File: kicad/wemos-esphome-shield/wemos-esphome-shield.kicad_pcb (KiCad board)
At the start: 2 copper layers, 74 x 52 mm, 28 parts, among them Q1 2N2222, Q2 2N2222, Q3 2N2222, T1 Transformer_1P_1S, U1 WeMos_D1_mini

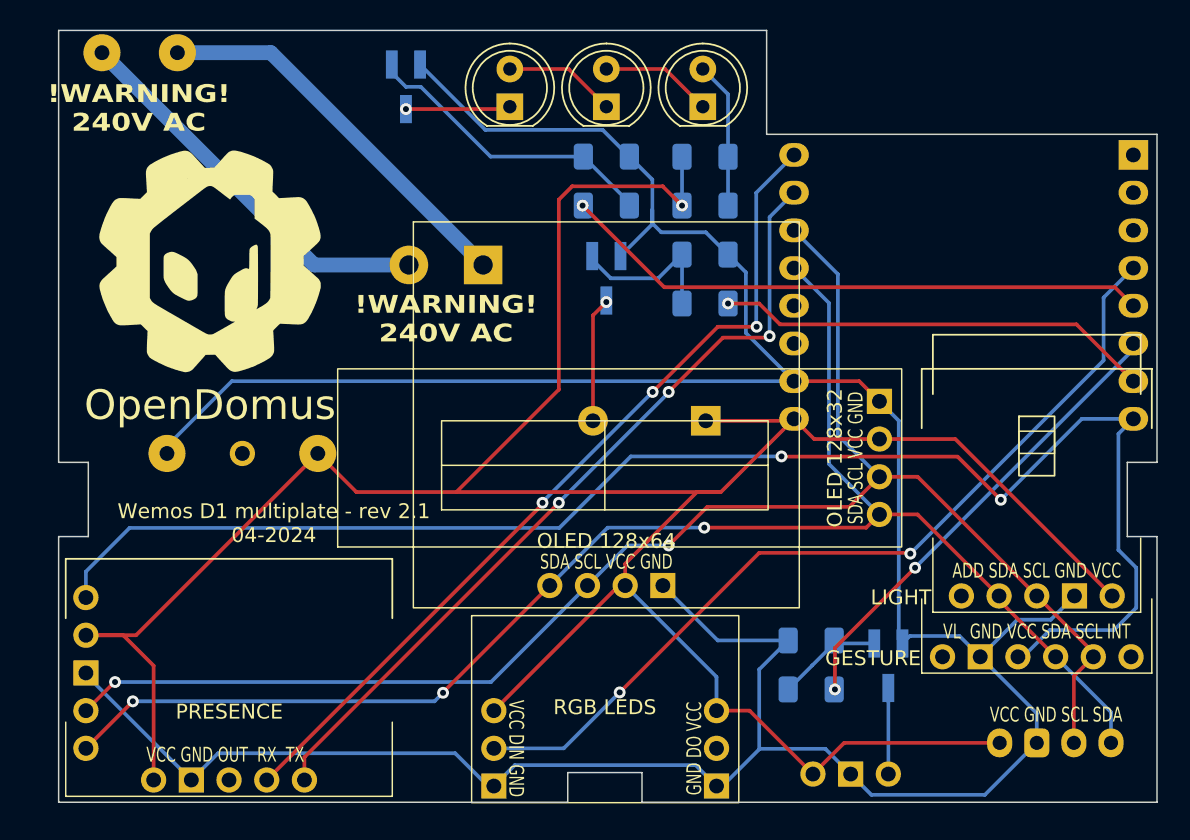
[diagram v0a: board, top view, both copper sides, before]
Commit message: move stuff around
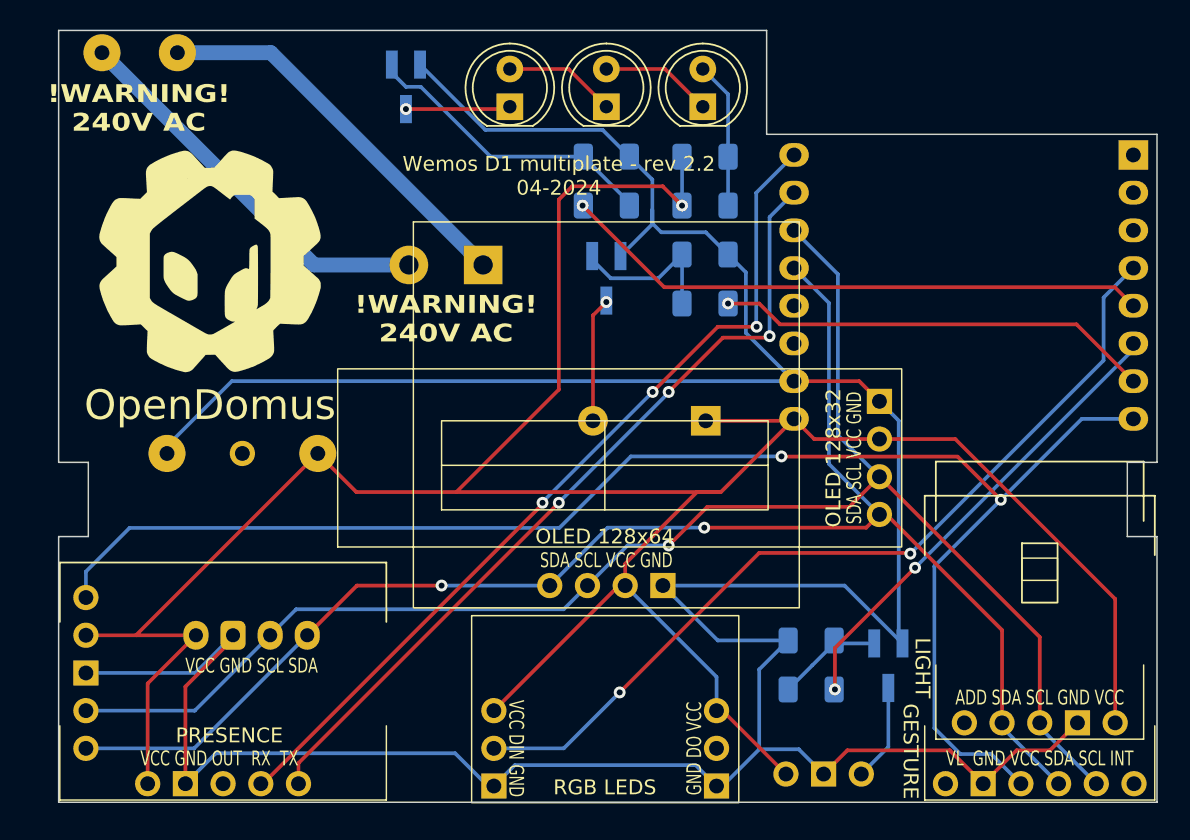
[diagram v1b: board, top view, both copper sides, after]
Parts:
- moved TEMP1 62.1 mm to (88.2, 104.8), turned to 0 degrees
- moved LUM1 8.55 mm to (145.1, 110.7)
- moved GEST1 8.55 mm to (145.1, 114.8)
- moved RELAY1 1.82 mm to (133.1, 114.1)
- moved MOV1 0.47 mm to (90.1, 114.8)
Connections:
- TEMP1 pad 1: SDA -> 5V
- TEMP1 pad 2: SCL -> GND
- TEMP1 pad 3: GND -> SCL
- TEMP1 pad 4: 5V -> SDA
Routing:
- net GND: track 222.3 -> 236.8 mm
- net 5V: track 192.7 -> 188.4 mm
- net 3.3V: track 102.0 -> 103.6 mm
- net SCL: track 104.9 -> 105.7 mm, vias 2 -> 1
- net Net-(Q2-C): track 5.80 -> 6.55 mm
- net SDA: vias 3 -> 2
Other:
- outline, holes or cut-outs redrawn
- board text added: "Wemos D1 multiplate - rev 2.2 04-2024"
- board text removed: "Wemos D1 multiplate - rev 2.1 04-2024"

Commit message: rev2.2 sent to jlcpcb
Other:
- board text added: "SDA SCL GND VCC"
- board text added: "TEMPERATURE/ HUMIDITY"
- board text removed: "TEMPERATURE"
- board text removed: "VCC GND SCL SDA"
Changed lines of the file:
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@@
     (effects (font (size 1 1) (thickness 0.15)) (justify right mirror))
   )
-  (gr_text "TEMPERATURE" (at 92 108.225) (layer "B.SilkS")
-    (effects (font (size 1 1) (thickness 0.15)) (justify mirror))
+  (gr_text "TEMPERATURE/\nHUMIDITY" (at 91.9 107.8) (layer "B.SilkS")
+    (effects (font (size 1 1) (thickness 0.15)) (justify top mirror))
   )
   (gr_text "RX" (at 129.8 75) (layer "B.SilkS")
@@
   (gr_text "3.3V" (at 150.3 90.2) (layer "B.SilkS")
     (effects (font (size 1 1) (thickness 0.15)) (justify left mirror))
+  )
+  (gr_text "SDA SCL GND VCC" (at 92 106.8) (layer "B.SilkS")
+    (effects (font (size 1 0.7) (thickness 0.15)) (justify mirror))
   )
   (gr_text "5V" (at 129.8 90.2) (layer "B.SilkS")
@@
     (effects (font (size 1 1) (thickness 0.15)) (justify right))
   )
-  (gr_text "VCC GND SCL SDA" (at 92 106.8) (layer "F.SilkS")
-    (effects (font (size 1 0.7) (thickness 0.15)))
-  )
   (gr_text "!WARNING!\n240V AC" (at 84.4 70.9) (layer "F.SilkS")

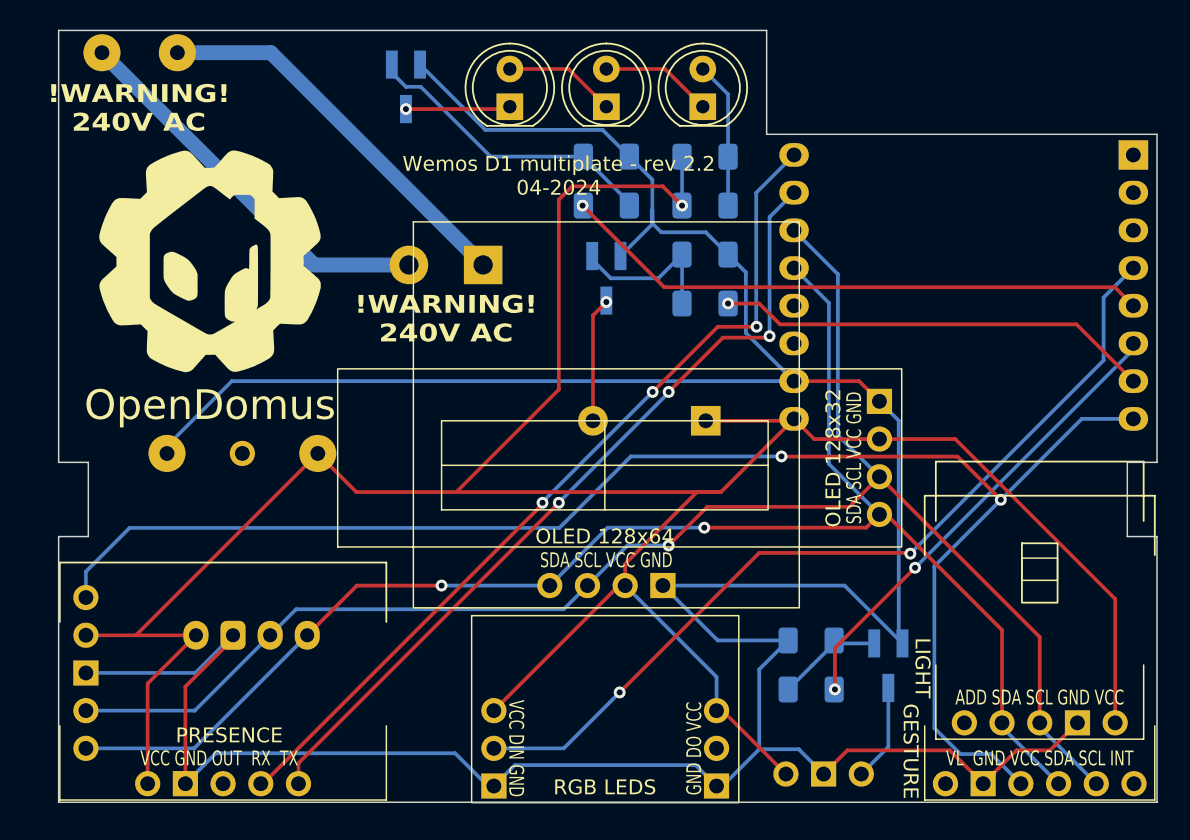
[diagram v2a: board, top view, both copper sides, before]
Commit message: fix some tracks
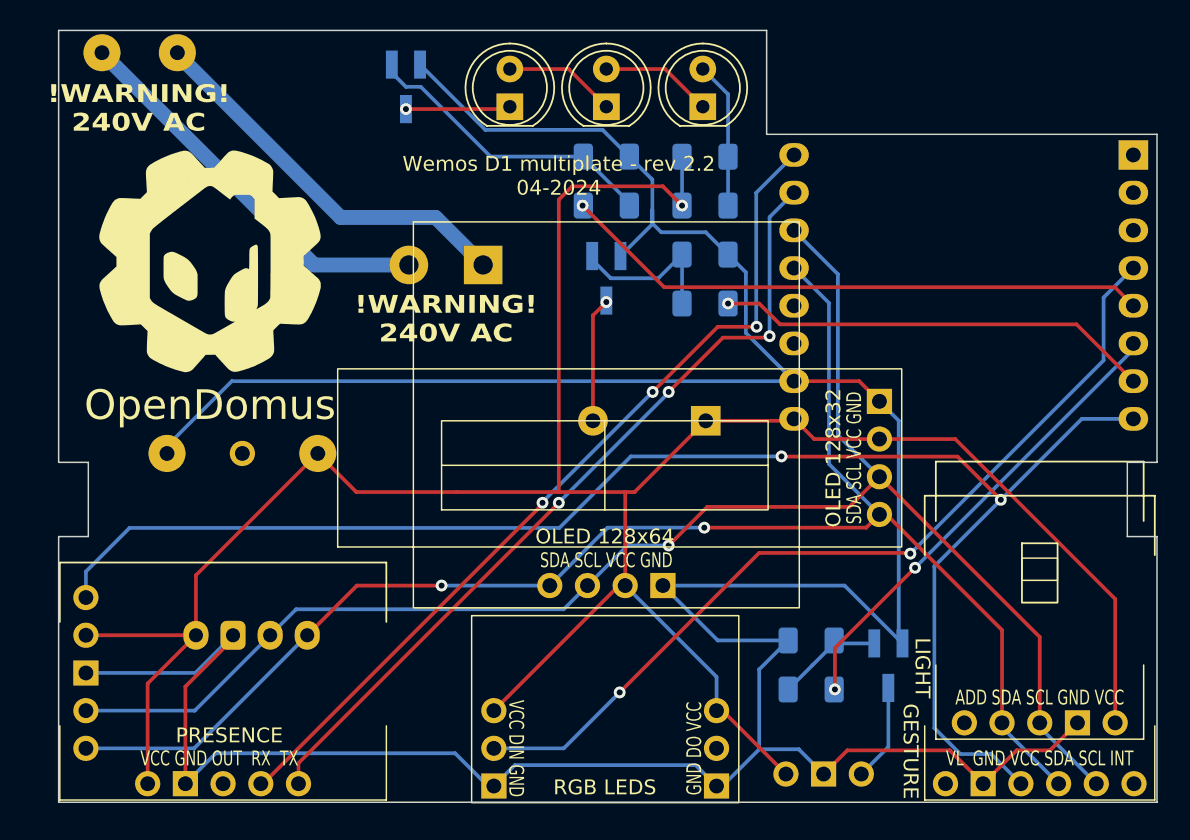
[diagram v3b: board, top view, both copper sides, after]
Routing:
- net 5V: track 188.4 -> 174.4 mm
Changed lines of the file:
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@@
   )
   (segment (start 150.18 110.65) (end 150.18 102.300001) (width 0.25) (layer "F.Cu") (net 1))
-  (segment (start 122 95.1) (end 123.4 95.1) (width 0.25) (layer "F.Cu") (net 1))
-  (segment (start 121 75.8) (end 119.7 74.5) (width 0.25) (layer "F.Cu") (net 1))
   (segment (start 123.728 109.828) (end 123.324 109.828) (width 0.25) (layer "F.Cu") (net 1))
   (segment (start 128.547 90.17) (end 129.29 90.17) (width 0.25) (layer "F.Cu") (net 1))
-  (segment (start 119.7 74.5) (end 113.6 74.5) (width 0.25) (layer "F.Cu") (net 1))
   (segment (start 139.409999 91.53) (end 134.3 91.53) (width 0.25) (layer "F.Cu") (net 1))
   (segment (start 134.3 91.53) (end 129.927 91.53) (width 0.25) (layer "F.Cu") (net 1))
-  (segment (start 123.617 95.1) (end 128.547 90.17) (width 0.25) (layer "F.Cu") (net 1))
   (segment (start 108.742 109.828) (end 107.924 109.828) (width 0.25) (layer "F.Cu") (net 1))
-  (segment (start 123.4 95.1) (end 123.617 95.1) (width 0.25) (layer "F.Cu") (net 1))
+  (segment (start 96.46 92.5) (end 88.25 100.71) (width 0.25) (layer "F.Cu") (net 1))
   (segment (start 129.917 91.54) (end 128.547 90.17) (width 0.25) (layer "F.Cu") (net 1))
+  (segment (start 117.8 95.1) (end 117.2 95.1) (width 0.25) (layer "F.Cu") (net 1))
+  (segment (start 112.7 75.4) (end 112.7 95.1) (width 0.25) (layer "F.Cu") (net 1))
   (segment (start 85 108) (end 88.25 104.75) (width 0.25) (layer "F.Cu") (net 1))
-  (segment (start 117.17 101.4) (end 117.17 99.93) (width 0.25) (layer "F.Cu") (net 1))
+  (segment (start 121 75.8) (end 119.7 74.5) (width 0.25) (layer "F.Cu") (net 1))
+  (segment (start 119.7 74.5) (end 113.6 74.5) (width 0.25) (layer "F.Cu") (net 1))
+  (segment (start 117.17 95.13) (end 117.14 95.1) (width 0.25) (layer "F.Cu") (net 1))
+  (segment (start 113.6 74.5) (end 112.7 75.4) (width 0.25) (layer "F.Cu") (net 1))
   (segment (start 129.927 91.53) (end 129.917 91.54) (width 0.25) (layer "F.Cu") (net 1))
+  (segment (start 117.17 101.4) (end 117.17 95.13) (width 0.25) (layer "F.Cu") (net 1))
   (segment (start 116.752 101.4) (end 117.17 101.4) (width 0.25) (layer "F.Cu") (net 1))
-  (segment (start 105.8 95.1) (end 123.4 95.1) (width 0.25) (layer "F.Cu") (net 1))
-  (segment (start 117.17 99.93) (end 122 95.1) (width 0.25) (layer "F.Cu") (net 1))
-  (segment (start 113.6 74.5) (end 112.7 75.4) (width 0.25) (layer "F.Cu") (net 1))
   (segment (start 150.18 102.300001) (end 139.409999 91.53) (width 0.25) (layer "F.Cu") (net 1))
+  (segment (start 117.2 95.1) (end 117.17 95.13) (width 0.25) (layer "F.Cu") (net 1))
   (segment (start 99.06 95.1) (end 105.8 95.1) (width 0.25) (layer "F.Cu") (net 1))
+  (segment (start 88.25 100.71) (end 88.25 104.75) (width 0.25) (layer "F.Cu") (net 1))
   (segment (start 122.6 90.3) (end 128.417 90.3) (width 0.25) (layer "F.Cu") (net 1))
   (segment (start 85 114.75) (end 85 108) (width 0.25) (layer "F.Cu") (net 1))
   (segment (start 96.46 92.5) (end 99.06 95.1) (width 0.25) (layer "F.Cu") (net 1))
+  (segment (start 117.14 95.1) (end 112.7 95.1) (width 0.25) (layer "F.Cu") (net 1))
   (segment (start 80.84 104.75) (end 80.838 104.748) (width 0.25) (layer "F.Cu") (net 1))
-  (segment (start 112.7 88.2) (end 105.8 95.1) (width 0.25) (layer "F.Cu") (net 1))
-  (segment (start 112.7 75.4) (end 112.7 88.2) (width 0.25) (layer "F.Cu") (net 1))
   (segment (start 108.324 109.828) (end 116.752 101.4) (width 0.25) (layer "F.Cu") (net 1))
-  (segment (start 96.46 92.5) (end 84.212 104.748) (width 0.25) (layer "F.Cu") (net 1))
+  (segment (start 112.7 95.1) (end 105.8 95.1) (width 0.25) (layer "F.Cu") (net 1))
   (segment (start 128.417 90.3) (end 128.547 90.17) (width 0.25) (layer "F.Cu") (net 1))
   (segment (start 128 114.1) (end 123.728 109.828) (width 0.25) (layer "F.Cu") (net 1))
+  (segment (start 122.6 90.3) (end 117.8 95.1) (width 0.25) (layer "F.Cu") (net 1))
   (segment (start 88.25 104.75) (end 80.84 104.75) (width 0.25) (layer "F.Cu") (net 1))
   (via (at 121 75.8) (size 0.8) (drill 0.4) (layers "F.Cu" "B.Cu") (net 1))
@@
   (segment (start 96.22 79.8) (end 102.6 79.8) (width 1) (layer "B.Cu") (net 10))
   (segment (start 81.92 65.5) (end 96.22 79.8) (width 1) (layer "B.Cu") (net 10))
-  (segment (start 93.3 65.5) (end 107.6 79.8) (width 1) (layer "B.Cu") (net 11))
-  (segment (start 87 65.5) (end 93.3 65.5) (width 1) (layer "B.Cu") (net 11))
+  (segment (start 87 65.5) (end 87 65.6) (width 1) (layer "B.Cu") (net 11))
+  (segment (start 98 76.6) (end 104.4 76.6) (width 1) (layer "B.Cu") (net 11))
+  (segment (start 87 65.6) (end 98 76.6) (width 1) (layer "B.Cu") (net 11))
+  (segment (start 104.4 76.6) (end 107.6 79.8) (width 1) (layer "B.Cu") (net 11))
   (segment (start 131.3 105.6) (end 136.7 100.2) (width 0.25) (layer "F.Cu") (net 12))
   (segment (start 131.3 108.4) (end 131.3 105.6) (width 0.25) (layer "F.Cu") (net 12))
